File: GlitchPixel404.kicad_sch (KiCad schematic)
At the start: 60 parts, among them J1 USB_C_Receptacle_USB2.0_16P, J2 VOLTLINK, J5 Barrel_Jack_Switch, J7 Output, Q1 AONR21357-ES, Q2 MMBT3904, SW1 Reset, SW2 Boot, SW3 SW_SP3T, SW4 USER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

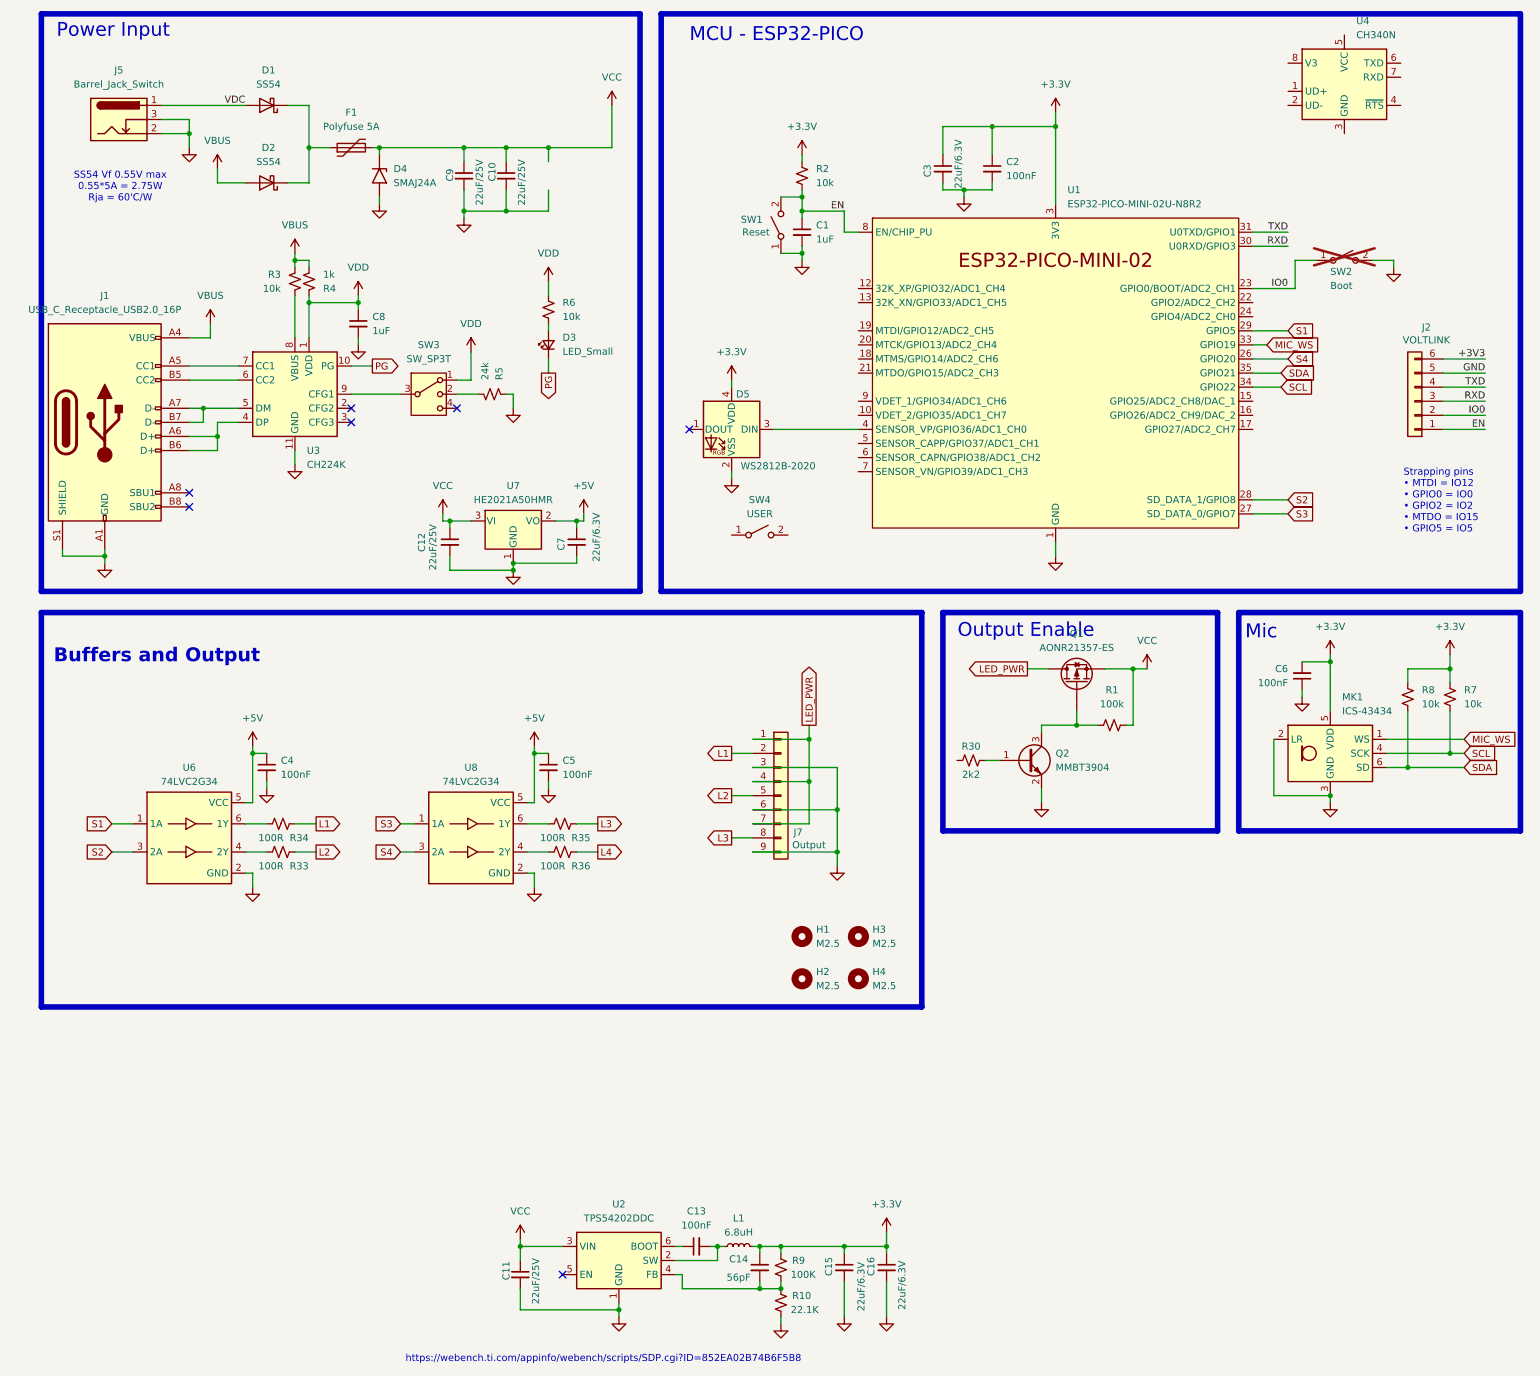
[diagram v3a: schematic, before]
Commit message: Parts selection and 0402
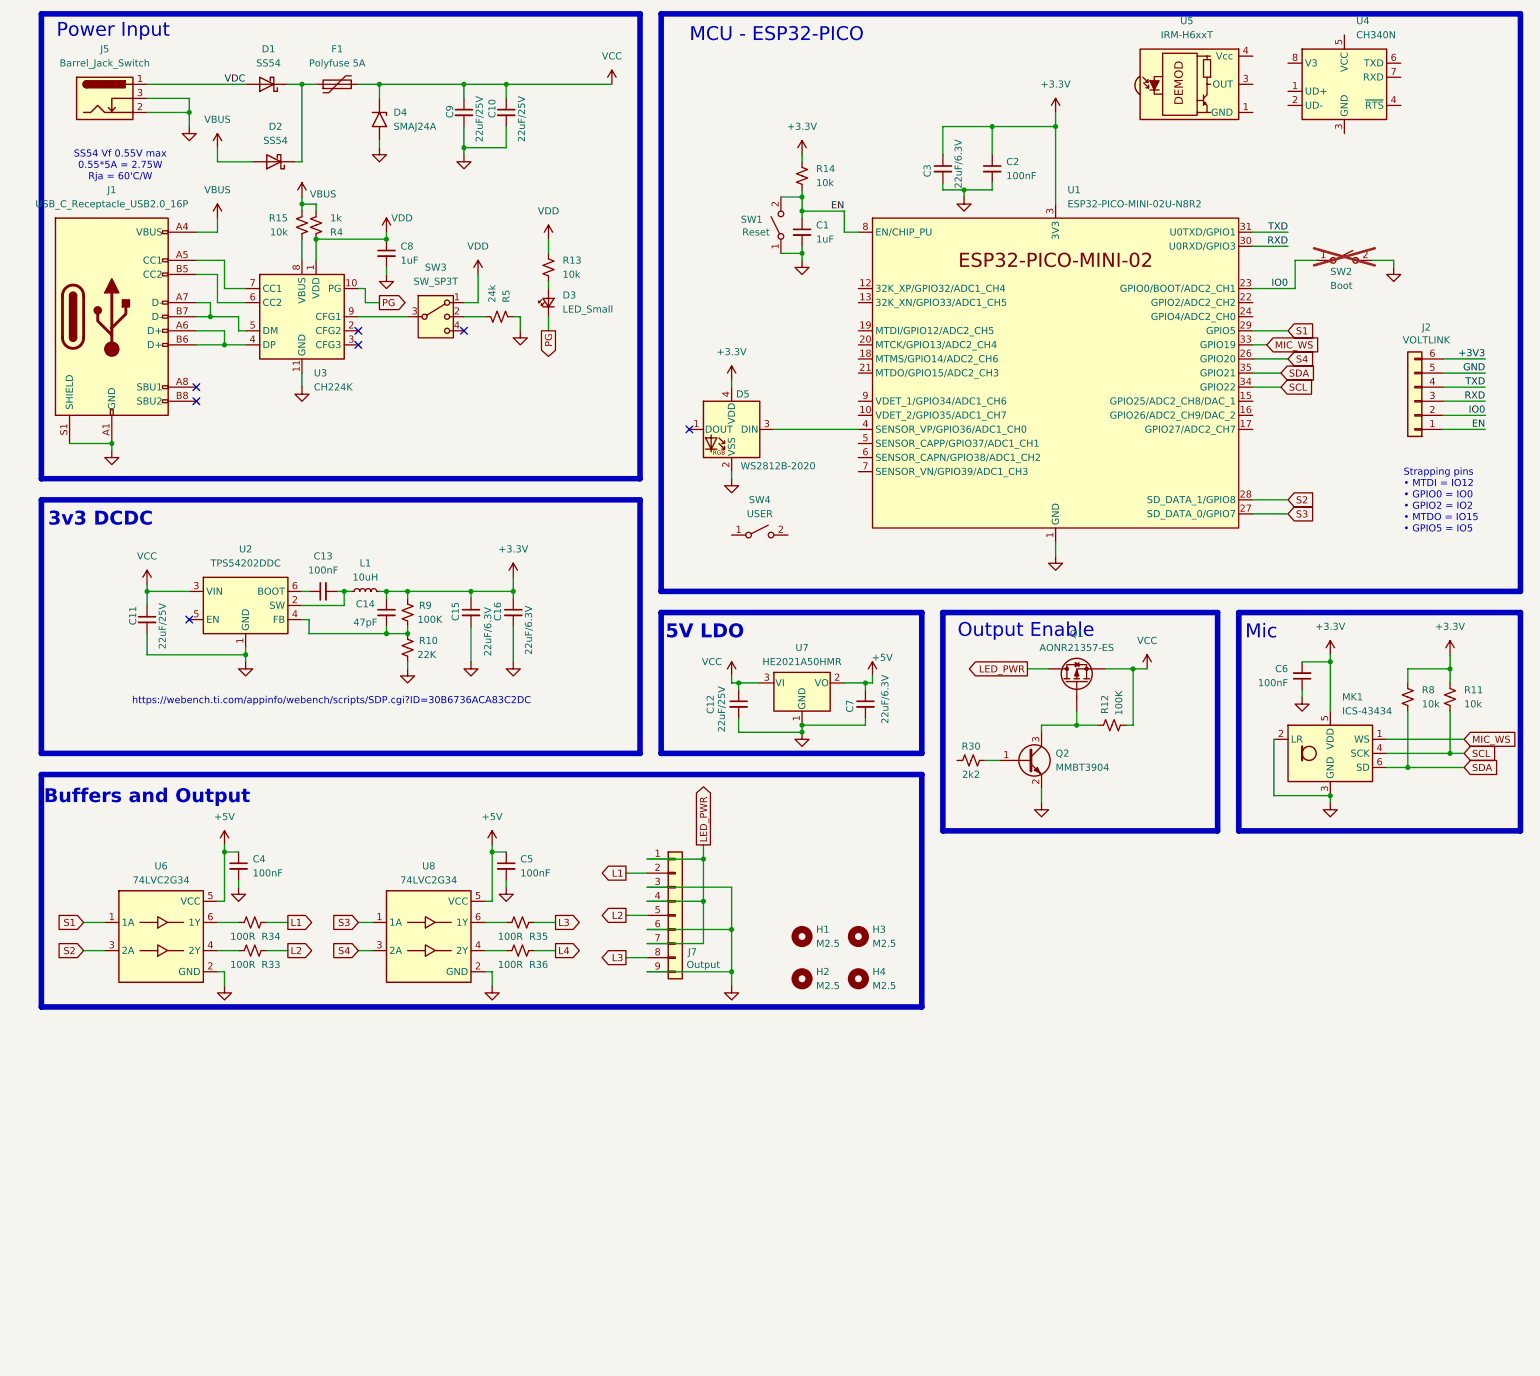
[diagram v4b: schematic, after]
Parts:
- removed R1: 100k, Resistor_SMD:R_0603_1608Metric, symbol Device:R_Small_US
- removed R2, R3, R6, R7: 10k, Resistor_SMD:R_0603_1608Metric, symbol Device:R_Small_US
- added R11, R13, R14, R15: 10k, Resistor_SMD:R_0402_1005Metric, symbol Device:R_Small_US
- added R12: 100K, Resistor_SMD:R_0402_1005Metric, symbol Device:R_Small_US
- added U5: IRM-H6xxT, OptoDevice:Everlight_IRM-H6xxT, symbol Interface_Optical:IRM-H6xxT
- C14: value 56pF -> 47pF; LCSC (none) -> C1567; MPN (none) -> 0402CG470J500NT; Volt (none) -> 50V
- L1: value 6.8uH -> 10uH; footprint (none) -> Inductor_SMD:L_Changjiang_FNR4018S; LCSC (none) -> C167808; MPN (none) -> FNR4018S100MT
- R10: value 22.1K -> 22K; LCSC (none) -> C25768; MPN (none) -> 0402WGF2202TCE
- R4: footprint Resistor_SMD:R_0603_1608Metric -> Resistor_SMD:R_0402_1005Metric; LCSC C21190 -> C11702; MPN 0603WAF1001T5E -> 0402WGF1001TCE
- R8: footprint Resistor_SMD:R_0603_1608Metric -> Resistor_SMD:R_0402_1005Metric; LCSC C25804 -> C25744; MPN (none) -> 0402WGF1002TCE
- R9: LCSC (none) -> C25741; MPN (none) -> 0402WGF1003TCE
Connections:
- net +3.3V: now also R11.1, R14.1
- net EN: now also R14.2
- net SCL: now also R11.2
- net VBUS: now also R15.1
- net VCC: now also R12.2
- net VDD: now also R13.1
- net at U3.8 (VBUS): now also R15.2
- net at D3.2 (A): now also R13.2
- net at Q1.G, Q2.3 (C): now also R12.1
- new net: U5.1 (GND), U5.2 (GND)
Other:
- note added: "3v3 DCDC"
- note added: "5V LDO"
- note added: "https://webench.ti.com/appinfo/webench/scripts/SDP.cgi?ID=30B6736ACA83C2DC"
- note removed: "https://webench.ti.com/appinfo/webench/scripts/SDP.cgi?ID=852EA02B74B6F5B8"
- moved on the sheet: C10, C11, C12, C13, C14, C15, C16, C4, C5, C7, C8, C9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
